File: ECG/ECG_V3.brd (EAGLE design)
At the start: 73.7 x 47 mm, 32 parts, among them U1 AD8232, U3 BGM111-VISUAL-A

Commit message: Added mounting holes
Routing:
- net GND: track 141.3 -> 143.7 mm
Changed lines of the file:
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@@
 <wire x1="7.62" y1="46.99" x2="46.99" y2="46.99" width="0.8128" layer="20"/>
 <wire x1="46.99" y1="46.99" x2="71.12" y2="22.86" width="0.8128" layer="20" curve="-90"/>
+<hole x="5.588" y="5.08" drill="1.5"/>
+<hole x="58.674" y="40.513" drill="1.5"/>
 </plain>
 <attributes>
@@
 <wire x1="24.2062" y1="27.2796" x2="24.5618" y2="26.924" width="0.1778" layer="1"/>
 <wire x1="24.5618" y1="26.924" x2="28.194" y2="26.924" width="0.1778" layer="1"/>
-<polygon width="0.1778" layer="1">
-<vertex x="-4.572" y="47.625"/>
-<vertex x="72.644" y="47.625"/>
-<vertex x="72.644" y="-0.127"/>
-<vertex x="-4.572" y="-0.127"/>
+<wire x1="28.194" y1="26.924" x2="28.51" y2="26.924" width="0.127" layer="1"/>
+<wire x1="28.51" y1="26.924" x2="28.51" y2="29.01" width="0.127" layer="1"/>
+<polygon width="0.127" layer="16">
+<vertex x="-4.953" y="48.514"/>
+<vertex x="75.565" y="48.514"/>
+<vertex x="75.565" y="-2.667"/>
+<vertex x="-4.826" y="-2.667"/>
+<vertex x="-4.826" y="-2.413"/>
+<vertex x="-4.953" y="-2.413"/>
 </polygon>
-<polygon width="0.1778" layer="16">
-<vertex x="-4.572" y="47.625"/>
-<vertex x="-4.572" y="-0.127"/>
-<vertex x="72.644" y="-0.127"/>
-<vertex x="72.644" y="47.625"/>
+<polygon width="0.127" layer="1">
+<vertex x="-4.826" y="48.514"/>
+<vertex x="75.565" y="48.514"/>
+<vertex x="75.565" y="40.767"/>
+<vertex x="75.565" y="37.465"/>
+<vertex x="75.565" y="5.207"/>
+<vertex x="75.565" y="4.572"/>
+<vertex x="75.565" y="-2.794"/>
+<vertex x="-4.826" y="-2.794"/>
 </polygon>
 </signal>

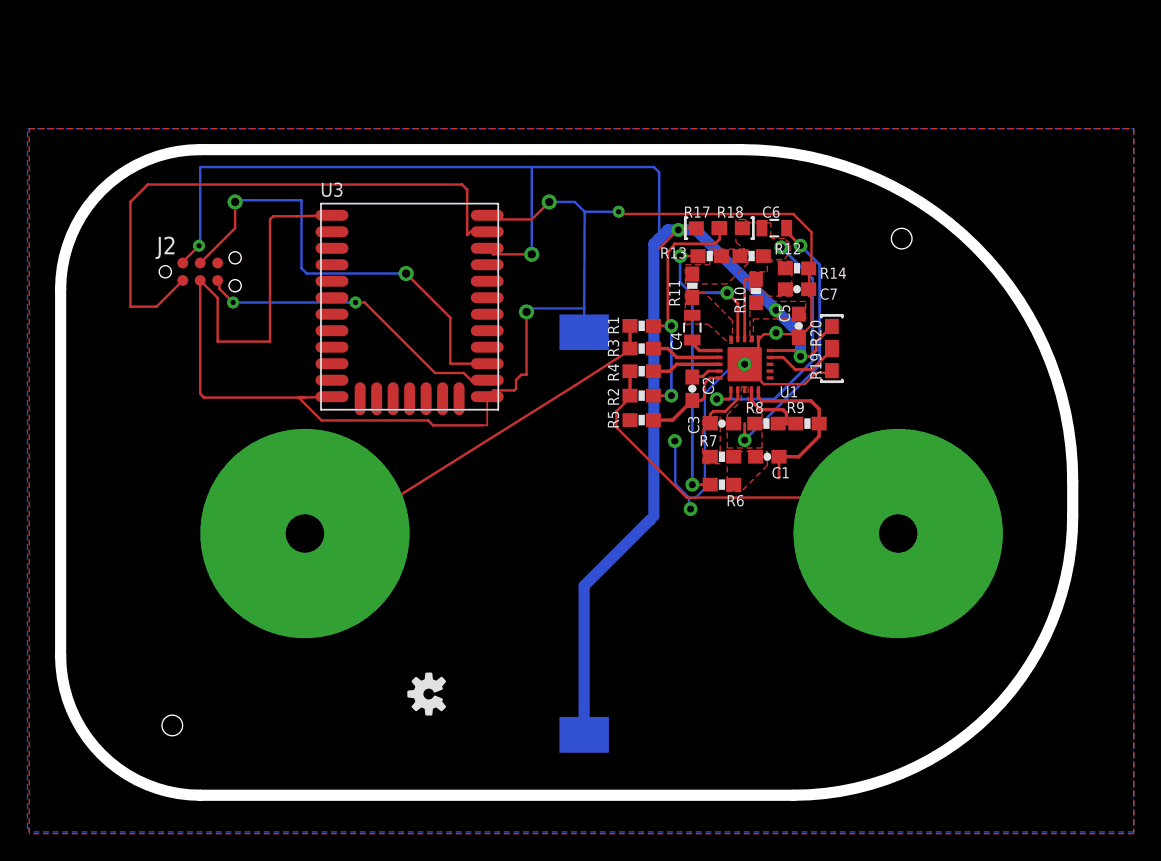
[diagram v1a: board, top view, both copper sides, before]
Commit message: Modified Sewtap pads and reduced board size
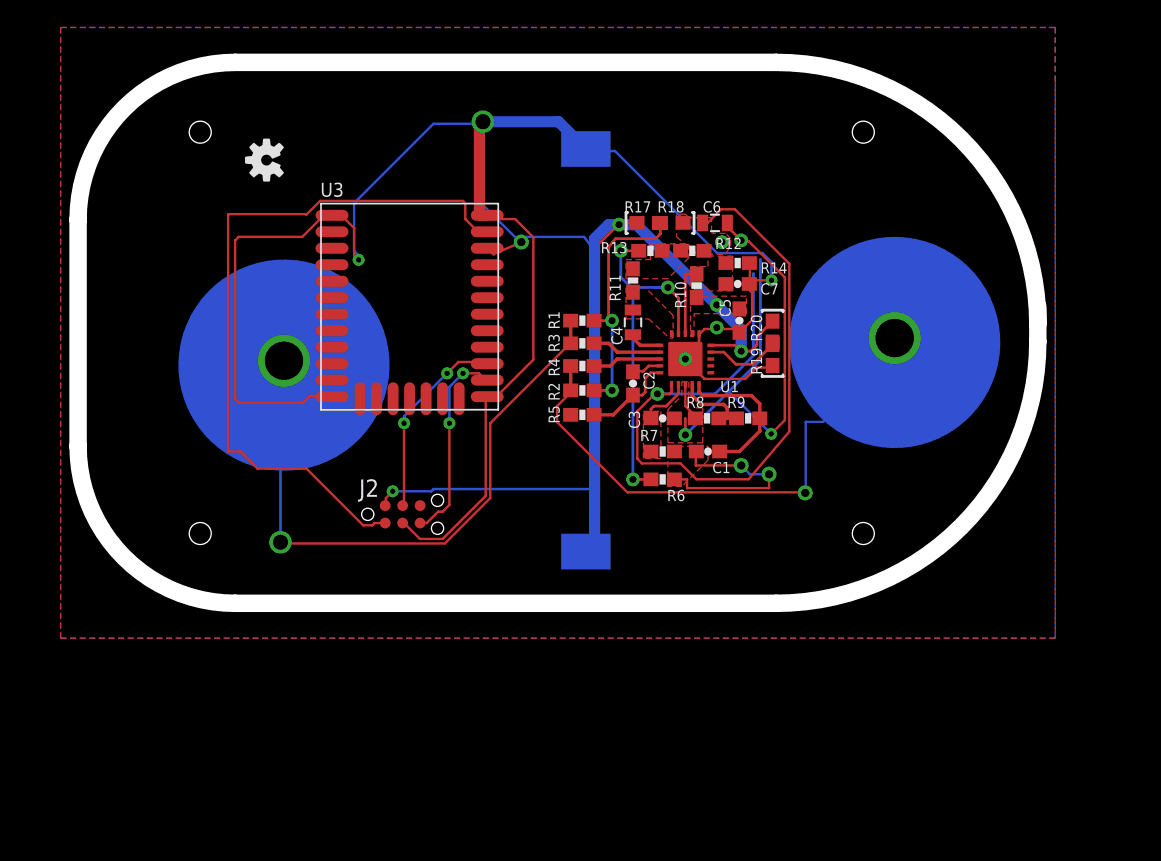
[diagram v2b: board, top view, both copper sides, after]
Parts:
- removed JP3, JP4: SEWTAP2, LilyPad-Wearables:PETAL-LONG-2
- added JP1, JP2: SEWTAP2, LilyPad-Wearables:PETAL-LONG-2
- moved LOGO1 40.6 mm to (12.4, 46.2)
- moved J2 23.0 mm to (19.8, 20.4)
- moved BAT1 13.3 mm to (35.7, 32.4)
- moved C1 4.33 mm to (44.6, 25.0)
- moved C3 4.33 mm to (41.3, 27.4)
- moved C7 4.33 mm to (46.7, 37.2)
- moved R12 4.33 mm to (43.4, 39.6)
- moved R14 4.33 mm to (46.7, 38.7)
- moved R18 4.33 mm to (41.9, 41.7)
- moved R6 4.33 mm to (41.3, 23.0)
- moved R7 4.33 mm to (41.3, 25.0)
- moved R9 4.33 mm to (47.5, 27.4)
- moved C2 4.33 mm to (39.1, 30.0)
- moved C4 4.33 mm to (39.1, 34.4)
- moved C5 4.33 mm to (46.9, 34.5)
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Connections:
- net LA: now also JP1.1; no longer JP3.1
- net RA: now also JP2.1; no longer JP4.1
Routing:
- net 3.3V: track 118.6 -> 79.5 mm
- net N$16: track 19.0 -> 55.1 mm
- net REFOUT: track 20.0 -> 41.4 mm, vias 2 -> 3
- net N$33: track 33.7 -> 14.3 mm
- net LA: track 29.3 -> 45.3 mm, vias 0 -> 1
- net N$9: track 0.00 -> 15.2 mm, vias 0 -> 2
- net RA: track 28.3 -> 39.2 mm, vias 0 -> 1
- net N$29: track 42.3 -> 51.9 mm
- net GND: track 143.7 -> 134.9 mm, vias 7 -> 5
- net N$31: track 23.0 -> 14.6 mm
- net SIGNAL_OUT: track 12.4 -> 10.8 mm
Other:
- board size 73.7 x 47 mm -> 69.8 x 39.4 mm
